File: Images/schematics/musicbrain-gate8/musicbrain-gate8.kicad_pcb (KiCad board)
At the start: 2 copper layers, 60 x 34 mm, 15 parts, among them J1 BUS, J2 GATES OUT, U1 74HCT595, U2 AMS1117-5.0

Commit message: Jack-printjes (jack8/jack4) + mechanica-standaard + silk-links
- jack8/jack4: Thonkiconn (PJ398SM) paneeldragers, sch+PCB volledig geroute
  (ERC 0, DRC 0/0); footprint naar clacktronics/AudioJacks-maten
  (T -4.92 / TN +3.38 / S +6.48, ovale sleufgaten 1.6x0.6)
- 1xN-contract identiek aan GATE8/ADC8-J2; female socket op achterzijde,
  headerhart op 44mm-standaard; TN-normalling via soldeerjumper JP1
  (dicht=inputs, OPEN bij outputs)
- spec: mechanica-standaard (haakse busconnector, frontconnector op 44mm,
  silk-linkschema musicbrain.nl/hw/<bord>); GATE8/ADC8 v1.1 volgt
- silk-links op gate8- en busboard-PCB bijgewerkt (DRC her-geverifieerd 0/0)

Co-Authored-By: Claude Fable 5 <noreply@anthropic.com>
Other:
- board text added: "musicbrain.nl/hw/gate8 rev 1.0"
- board text removed: "GATE8 rev 1.0"
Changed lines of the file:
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@@
     (stroke (width 0.1) (type default)) (fill none)
     (layer "Edge.Cuts"))
-  (gr_text "GATE8 rev 1.0" (at 146 133 0) (layer "F.SilkS")
+  (gr_text "musicbrain.nl/hw/gate8 rev 1.0" (at 138 133 0) (layer "F.SilkS")
     (effects (font (size 1 1) (thickness 0.15))))
   (zone (net 3) (net_name "GND") (layer "F.Cu")

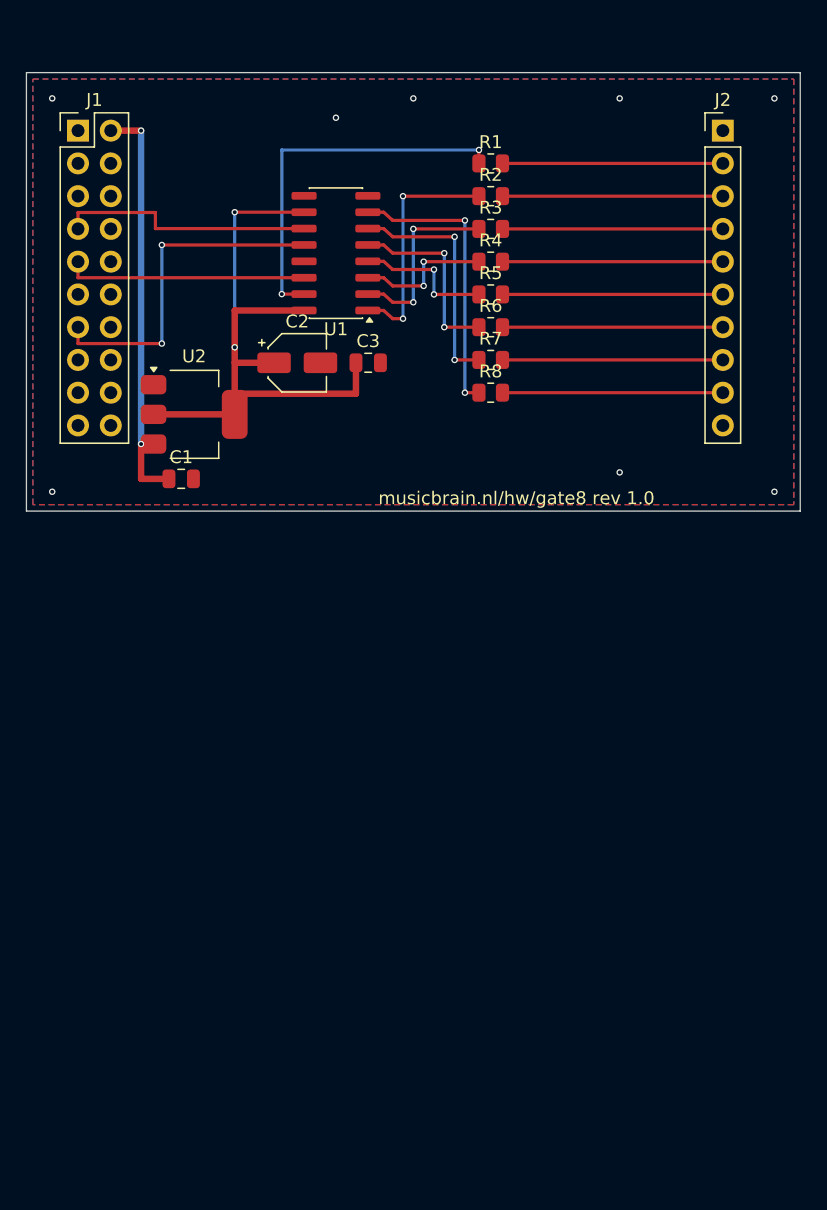
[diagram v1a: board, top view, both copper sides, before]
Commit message: GATE8 v1.1: H=80mm + haakse connectoren (bovenplaat-standaard)
- bord van 60x34 naar 35x80 mm (standaard-kaarthoogte H=80)
- J1 = haakse male 2x10 aan de onderrand (pennen het slot in),
  J2 = haakse male 1x10 aan de bovenrand, gecentreerd boven J1
- volledig opnieuw geroute: Q-netten als kruisingsvrije B.Cu-L-paden,
  SCLK/CS elk 1 B-hop, +5V-distributie via B-run; DRC 0/0, netlijst
  pad-voor-pad geverifieerd tegen het schema

Co-Authored-By: Claude Fable 5 <noreply@anthropic.com>
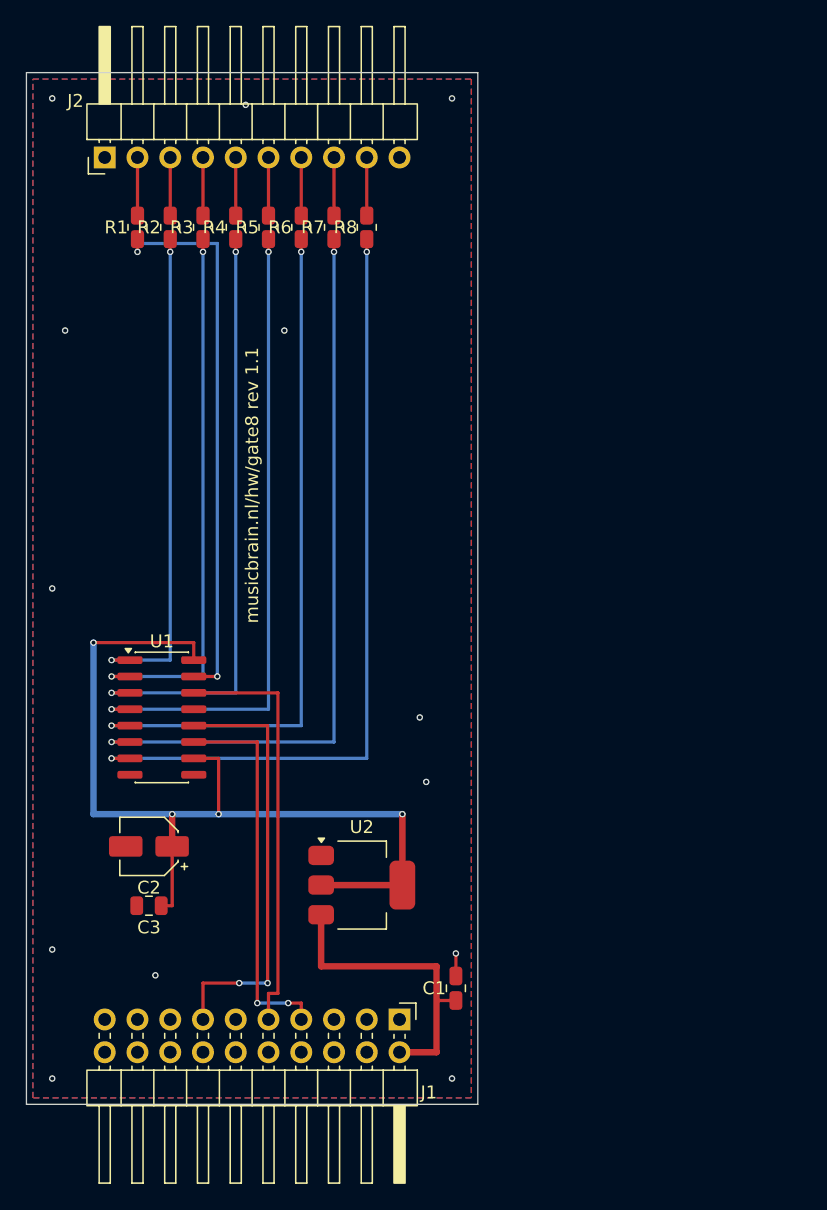
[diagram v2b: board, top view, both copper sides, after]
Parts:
- C1: renamed from C2; value 10u -> 100n; footprint Capacitor_SMD:CP_Elec_4x5.3 -> Capacitor_SMD:C_0805_2012Metric
- C2: renamed from C3; value 100n -> 10u; footprint Capacitor_SMD:C_0805_2012Metric -> Capacitor_SMD:CP_Elec_4x5.3
- C3: renamed from J2; value GATES OUT -> 100n; footprint Connector_PinHeader_2.54mm:PinHeader_1x10_P2.54mm_Vertical -> Capacitor_SMD:C_0805_2012Metric
- J1: footprint Connector_PinHeader_2.54mm:PinHeader_2x10_P2.54mm_Vertical -> Connector_PinHeader_2.54mm:PinHeader_2x10_P2.54mm_Horizontal
- J2: renamed from U1; value 74HCT595 -> GATES OUT; footprint Package_SO:SOIC-16_3.9x9.9mm_P1.27mm -> Connector_PinHeader_2.54mm:PinHeader_1x10_P2.54mm_Horizontal
- U1: renamed from U2; value AMS1117-5.0 -> 74HCT595; footprint Package_TO_SOT_SMD:SOT-223-3_TabPin2 -> Package_SO:SOIC-16_3.9x9.9mm_P1.27mm
- U2: renamed from C1; value 100n -> AMS1117-5.0; footprint Capacitor_SMD:C_0805_2012Metric -> Package_TO_SOT_SMD:SOT-223-3_TabPin2
- moved C3 74.8 mm to (109.5, 164.6), turned to 180 degrees
- moved J1 73.3 mm to (128.9, 173.4), turned to 270 degrees
- moved C1 50.0 mm to (133.3, 171.0), turned to 90 degrees
- moved C2 41.2 mm to (109.5, 160.0), turned to 180 degrees
- moved U2 34.5 mm to (126.0, 163.0)
- moved R1 27.8 mm to (108.6, 112.0), turned to 90 degrees
- moved R2 25.0 mm to (111.2, 112.0), turned to 90 degrees
- moved U1 23.6 mm to (110.5, 150.0)
- moved R3 22.3 mm to (113.7, 112.0), turned to 90 degrees
- moved R4 19.9 mm to (116.2, 112.0), turned to 90 degrees
- moved J2 19.4 mm to (106.1, 106.6), turned to 90 degrees
- moved R5 18.0 mm to (118.8, 112.0), turned to 90 degrees
- moved R6 16.6 mm to (121.3, 112.0), turned to 90 degrees
- moved R8 16.0 mm to (126.4, 112.0), turned to 90 degrees
- moved R7 15.9 mm to (123.8, 112.0), turned to 90 degrees
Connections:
- C1 pad 1: +5V -> +12V
- C3 pad 1: GND -> +5V
- C3 pad 2: /GATE1 -> GND
- J2 pad 1: Net-(U1-QB) -> GND
- J2 pad 10: +5V -> GND
- J2 pad 2: Net-(U1-QC) -> /GATE1
- J2 pad 3: Net-(U1-QD) -> /GATE2
- J2 pad 4: Net-(U1-QE) -> /GATE3
- J2 pad 5: Net-(U1-QF) -> /GATE4
- J2 pad 6: Net-(U1-QG) -> /GATE5
- J2 pad 7: Net-(U1-QH) -> /GATE6
- J2 pad 8: GND -> /GATE7
- J2 pad 9: (no net) -> /GATE8
- U1 pad 1: GND -> Net-(U1-QB)
- U1 pad 2: +5V -> Net-(U1-QC)
- U1 pad 3: +12V -> Net-(U1-QD)
- U2 pad 1: +12V -> GND
- U2 pad 2: GND -> +5V
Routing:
- net Net-(U1-QH): track 22.2 -> 61.5 mm
- net Net-(U1-QE): track 10.8 -> 50.0 mm
- net Net-(U1-QG): track 18.4 -> 57.7 mm
- net Net-(U1-QF): track 14.6 -> 53.9 mm
- net Net-(U1-QD): track 10.7 -> 46.2 mm
- net Net-(U1-QC): track 14.5 -> 42.4 mm
- net +5V: track 50.4 -> 72.4 mm, vias 2 -> 4
- net Net-(U1-QB): track 18.4 -> 38.6 mm
- net Net-(U1-QA): track 29.2 -> 43.2 mm
- net /MOSI: track 18.8 -> 32.6 mm
- net /GATE8: track 17.1 -> 4.51 mm
- net /GATE7: track 17.1 -> 4.51 mm
- net /GATE6: track 17.1 -> 4.51 mm
- net /GATE5: track 17.1 -> 4.51 mm
- net /GATE4: track 17.1 -> 4.51 mm
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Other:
- board size 60 x 34 mm -> 35 x 80 mm
- board text added: "musicbrain.nl/hw/gate8 rev 1.1"
- board text removed: "musicbrain.nl/hw/gate8 rev 1.0"
